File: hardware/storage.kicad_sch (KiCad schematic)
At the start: 9 parts, among them J7 Micro_SD_Card_Det1, U15 EMMC5.1_BGA153

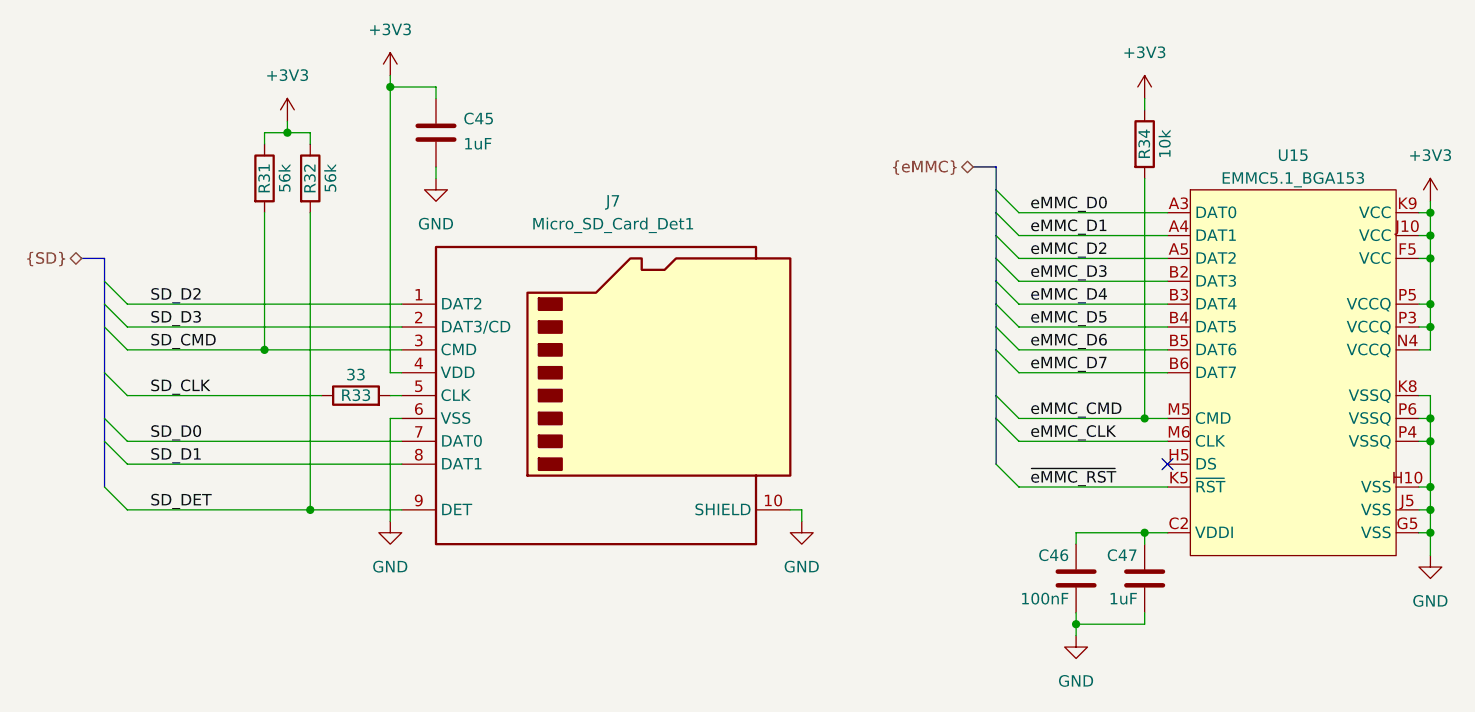
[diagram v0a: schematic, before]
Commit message: Finished DC DC converters and started decoupling the CPU
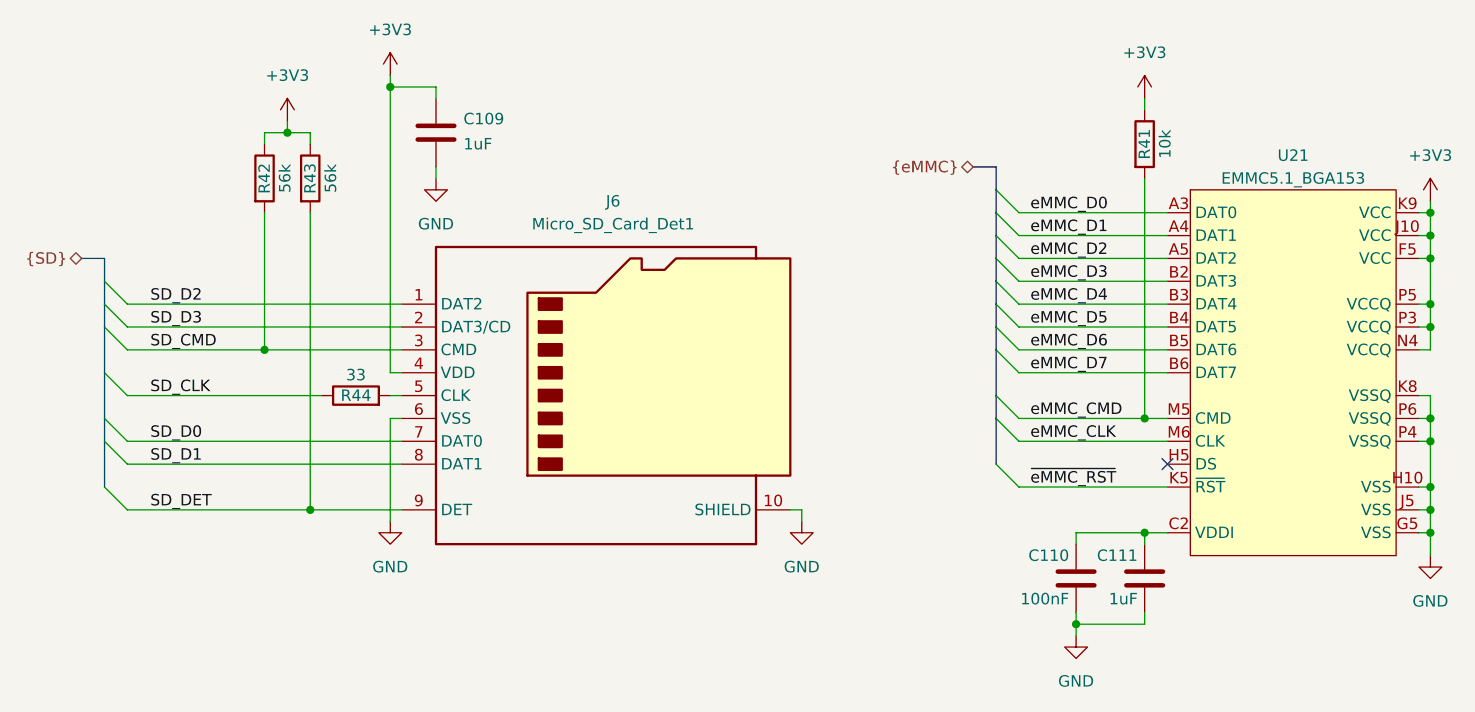
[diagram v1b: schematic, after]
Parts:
- renumbered C45 to C109, C46 to C110, C47 to C111, J7 to J6, R34 to R41, R31 to R42, R32 to R43, R33 to R44, U15 to U21
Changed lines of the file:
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@@
 		(dnp no)
 		(fields_autoplaced yes)
-		(property "Reference" "#PWR070"
+		(property "Reference" "#PWR0132"
 			(at 101.6 81.28 0)
 			(effects
@@
 			(project "cm0"
 				(path "/b53f5dbb-8078-4818-9e8f-fdf90ba6d854/bbbf0a3c-34ab-4b2d-85d9-faf7e9a88445"
-					(reference "#PWR070")
+					(reference "#PWR0132")
 					(unit 1)
 				)
@@
 		(on_board yes)
 		(dnp no)
-		(property "Reference" "C47"
+		(property "Reference" "C111"
 			(at 179.578 116.84 0)
 			(effects
@@
 			(project "cm0"
 				(path "/b53f5dbb-8078-4818-9e8f-fdf90ba6d854/bbbf0a3c-34ab-4b2d-85d9-faf7e9a88445"
-					(reference "C47")
+					(reference "C111")
 					(unit 1)
 				)
@@
 		(dnp no)
 		(fields_autoplaced yes)
-		(property "Reference" "#PWR073"
+		(property "Reference" "#PWR0130"
 			(at 180.34 69.85 0)
 			(effects
@@
 			(project ""
 				(path "/b53f5dbb-8078-4818-9e8f-fdf90ba6d854/bbbf0a3c-34ab-4b2d-85d9-faf7e9a88445"
-					(reference "#PWR073")
+					(reference "#PWR0130")
 					(unit 1)
 				)
@@
 		(on_board yes)
 		(dnp no)
-		(property "Reference" "R34"
+		(property "Reference" "R41"
 			(at 180.34 71.12 90)
 			(effects
@@
 			(project "cm0"
 				(path "/b53f5dbb-8078-4818-9e8f-fdf90ba6d854/bbbf0a3c-34ab-4b2d-85d9-faf7e9a88445"
-					(reference "R34")
+					(reference "R41")
 					(unit 1)
 				)
@@
 		(on_board yes)
 		(dnp no)
-		(property "Reference" "R31"
+		(property "Reference" "R42"
 			(at 82.55 74.93 90)
 			(effects
@@
 			(project "cm0"
 				(path "/b53f5dbb-8078-4818-9e8f-fdf90ba6d854/bbbf0a3c-34ab-4b2d-85d9-faf7e9a88445"
-					(reference "R31")
+					(reference "R42")
 					(unit 1)
 				)
@@
 		(on_board yes)
 		(dnp no)
-		(property "Reference" "C46"
+		(property "Reference" "C110"
 			(at 171.958 116.84 0)
 			(effects
@@
 			(project "cm0"
 				(path "/b53f5dbb-8078-4818-9e8f-fdf90ba6d854/bbbf0a3c-34ab-4b2d-85d9-faf7e9a88445"
-					(reference "C46")
+					(reference "C110")
 					(unit 1)
 				)
@@
 		(dnp no)
 		(fields_autoplaced yes)
-		(property "Reference" "#PWR071"
+		(property "Reference" "#PWR0135"
 			(at 142.24 119.38 0)
 			(effects
@@
 			(project ""
 				(path "/b53f5dbb-8078-4818-9e8f-fdf90ba6d854/bbbf0a3c-34ab-4b2d-85d9-faf7e9a88445"
-					(reference "#PWR071")
+					(reference "#PWR0135")
 					(unit 1)
 				)
@@
 		(dnp no)
 		(fields_autoplaced yes)
-		(property "Reference" "J7"
+		(property "Reference" "J6"
 			(at 121.285 77.47 0)
 			(effects
@@
 			(project ""
 				(path "/b53f5dbb-8078-4818-9e8f-fdf90ba6d854/bbbf0a3c-34ab-4b2d-85d9-faf7e9a88445"
-					(reference "J7")
+					(reference "J6")
 					(unit 1)
 				)
@@
 		(dnp no)
 		(fields_autoplaced yes)
-		(property "Reference" "#PWR074"
+		(property "Reference" "#PWR0133"
 			(at 212.09 81.28 0)
 			(effects
@@
 			(project "cm0"
 				(path "/b53f5dbb-8078-4818-9e8f-fdf90ba6d854/bbbf0a3c-34ab-4b2d-85d9-faf7e9a88445"
-					(reference "#PWR074")
+					(reference "#PWR0133")
 					(unit 1)
 				)
@@
 		(dnp no)
 		(fields_autoplaced yes)
-		(property "Reference" "#PWR069"
+		(property "Reference" "#PWR0134"
 			(at 96.52 119.38 0)
 			(effects
@@
 			(project ""
 				(path "/b53f5dbb-8078-4818-9e8f-fdf90ba6d854/bbbf0a3c-34ab-4b2d-85d9-faf7e9a88445"
-					(reference "#PWR069")
+					(reference "#PWR0134")
 					(unit 1)
 				)
@@
 		(dnp no)
 		(fields_autoplaced yes)
-		(property "Reference" "#PWR067"
+		(property "Reference" "#PWR0131"
 			(at 85.09 72.39 0)
 			(effects
@@
 			(project ""
 				(path "/b53f5dbb-8078-4818-9e8f-fdf90ba6d854/bbbf0a3c-34ab-4b2d-85d9-faf7e9a88445"
-					(reference "#PWR067")
+					(reference "#PWR0131")
 					(unit 1)
 				)
@@
 		(on_board yes)
 		(dnp no)
-		(property "Reference" "R33"
+		(property "Reference" "R44"
 			(at 92.71 99.06 90)
 			(effects
@@
 			(project "cm0"
 				(path "/b53f5dbb-8078-4818-9e8f-fdf90ba6d854/bbbf0a3c-34ab-4b2d-85d9-faf7e9a88445"
-					(reference "R33")
+					(reference "R44")
 					(unit 1)
 				)
@@
 		(dnp no)
 		(fields_autoplaced yes)
-		(property "Reference" "#PWR068"
+		(property "Reference" "#PWR0129"
 			(at 96.52 67.31 0)
 			(effects
@@
 			(project "cm0"
 				(path "/b53f5dbb-8078-4818-9e8f-fdf90ba6d854/bbbf0a3c-34ab-4b2d-85d9-faf7e9a88445"
-					(reference "#PWR068")
+					(reference "#PWR0129")
 					(unit 1)
 				)
@@
 		(dnp no)
 		(fields_autoplaced yes)
-		(property "Reference" "#PWR075"
+		(property "Reference" "#PWR0136"
 			(at 212.09 123.19 0)
 			(effects
@@
 			(project "cm0"
 				(path "/b53f5dbb-8078-4818-9e8f-fdf90ba6d854/bbbf0a3c-34ab-4b2d-85d9-faf7e9a88445"
-					(reference "#PWR075")
+					(reference "#PWR0136")
 					(unit 1)
 				)
@@
 		(dnp no)
 		(fields_autoplaced yes)
-		(property "Reference" "#PWR072"
+		(property "Reference" "#PWR0137"
 			(at 172.72 132.08 0)
 			(effects
@@
 			(project ""
 				(path "/b53f5dbb-8078-4818-9e8f-fdf90ba6d854/bbbf0a3c-34ab-4b2d-85d9-faf7e9a88445"
-					(reference "#PWR072")
+					(reference "#PWR0137")
 					(unit 1)
 				)
@@
 		(on_board yes)
 		(dnp no)
-		(property "Reference" "R32"
+		(property "Reference" "R43"
 			(at 87.63 74.93 90)
 			(effects
@@
 			(project "cm0"
 				(path "/b53f5dbb-8078-4818-9e8f-fdf90ba6d854/bbbf0a3c-34ab-4b2d-85d9-faf7e9a88445"
-					(reference "R32")
+					(reference "R43")
 					(unit 1)
 				)
@@
 		(dnp no)
 		(fields_autoplaced yes)
-		(property "Reference" "U15"
+		(property "Reference" "U21"
 			(at 196.85 72.39 0)
 			(effects
@@
 			(project ""
 				(path "/b53f5dbb-8078-4818-9e8f-fdf90ba6d854/bbbf0a3c-34ab-4b2d-85d9-faf7e9a88445"
-					(reference "U15")
+					(reference "U21")
 					(unit 1)
 				)
@@
 		(on_board yes)
 		(dnp no)
-		(property "Reference" "C45"
+		(property "Reference" "C109"
 			(at 104.648 68.326 0)
 			(effects
@@
 			(project "cm0"
 				(path "/b53f5dbb-8078-4818-9e8f-fdf90ba6d854/bbbf0a3c-34ab-4b2d-85d9-faf7e9a88445"
-					(reference "C45")
-					(unit 1)
-				)
+					(reference "C109")
+					(unit 1)
+				)

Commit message: Decoupling on PCB side almost done
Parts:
- J6: FT Position Offset (none) -> -1.905,0
- R44: LCSC Part # (none) -> C25105
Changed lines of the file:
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@@
+			)
+		)
+		(property "FT Position Offset" ""
+			(at 180.34 119.38 0)
+			(effects
+				(font
+					(size 1.27 1.27)
+				)
+				(hide yes)
+			)
+		)
+		(property "FT Rotation Offset" ""
+			(at 180.34 119.38 0)
+			(effects
+				(font
+					(size 1.27 1.27)
+				)
+				(hide yes)
 			)
 		)
@@
 			)
 		)
+		(property "FT Position Offset" ""
+			(at 180.34 71.12 90)
+			(effects
+				(font
+					(size 1.27 1.27)
+				)
+				(hide yes)
+			)
+		)
+		(property "FT Rotation Offset" ""
+			(at 180.34 71.12 90)
+			(effects
+				(font
+					(size 1.27 1.27)
+				)
+				(hide yes)
+			)
+		)
 		(pin "1"
 		)
@@
 		)
 		(property "LCSC Part #" "C25796"
+			(at 82.55 74.93 90)
+			(effects
+				(font
+					(size 1.27 1.27)
+				)
+				(hide yes)
+			)
+		)
+		(property "FT Position Offset" ""
+			(at 82.55 74.93 90)
+			(effects
+				(font
+					(size 1.27 1.27)
+				)
+				(hide yes)
+			)
+		)
+		(property "FT Rotation Offset" ""
 			(at 82.55 74.93 90)
 			(effects
@@
 			)
 		)
+		(property "FT Position Offset" ""
+			(at 172.72 119.38 0)
+			(effects
+				(font
+					(size 1.27 1.27)
+				)
+				(hide yes)
+			)
+		)
+		(property "FT Rotation Offset" ""
+			(at 172.72 119.38 0)
+			(effects
+				(font
+					(size 1.27 1.27)
+				)
+				(hide yes)
+			)
+		)
 		(pin "2"
 		)
@@
 			)
 		)
+		(property "FT Position Offset" "-1.905,0"
+			(at 120.65 99.06 0)
+			(effects
+				(font
+					(size 1.27 1.27)
+				)
+				(hide yes)
+			)
+		)
+		(property "FT Rotation Offset" ""
+			(at 120.65 99.06 0)
+			(effects
+				(font
+					(size 1.27 1.27)
+				)
+				(hide yes)
+			)
+		)
 		(pin "9"
 		)
@@
 			)
 		)
-		(property "LCSC Part #" ""
+		(property "LCSC Part #" "C25105"
+			(at 92.71 99.06 90)
+			(effects
+				(font
+					(size 1.27 1.27)
+				)
+				(hide yes)
+			)
+		)
+		(property "FT Position Offset" ""
+			(at 92.71 99.06 90)
+			(effects
+				(font
+					(size 1.27 1.27)
+				)
+				(hide yes)
+			)
+		)
+		(property "FT Rotation Offset" ""
 			(at 92.71 99.06 90)
 			(effects
@@
 			)
 		)
+		(property "FT Position Offset" ""
+			(at 87.63 74.93 90)
+			(effects
+				(font
+					(size 1.27 1.27)
+				)
+				(hide yes)
+			)
+		)
+		(property "FT Rotation Offset" ""
+			(at 87.63 74.93 90)
+			(effects
+				(font
+					(size 1.27 1.27)
+				)
+				(hide yes)
+			)
+		)
 		(pin "1"
 		)
@@
 			)
 		)
+		(property "FT Position Offset" ""
+			(at 196.85 96.52 0)
+			(effects
+				(font
+					(size 1.27 1.27)
+				)
+				(hide yes)
+			)
+		)
+		(property "FT Rotation Offset" ""
+			(at 196.85 96.52 0)
+			(effects
+				(font
+					(size 1.27 1.27)
+				)
+				(hide yes)
+			)
+		)
 		(pin "B6"
 		)
@@
 			(at 101.6 69.85 0)
 			(effects
+				(font
+					(size 1.27 1.27)
+				)
+				(hide yes)
+			)
+		)
+		(property "FT Position Offset" ""
+			(at 101.6 69.85 0)
+			(effects
+				(font
+					(size 1.27 1.27)
+				)
+				(hide yes)
+			)
+		)
+		(property "FT Rotation Offset" ""
+			(at 101.6 69.85 0)
+			(effects

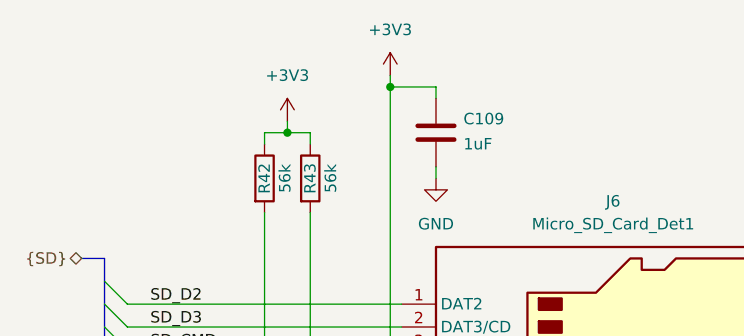
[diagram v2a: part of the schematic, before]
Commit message: Routed DCDC, EPHY and SD
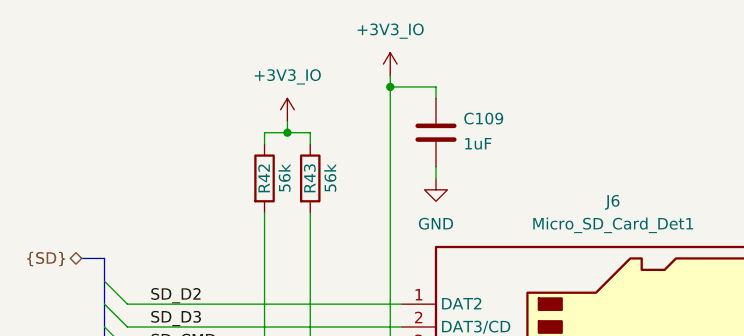
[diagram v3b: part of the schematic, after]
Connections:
- net +3V3: no longer C109.2, J6.4 (VDD), R42.1, R43.1
- new net +3V3_IO: C109.2, J6.4 (VDD), R42.1, R43.1
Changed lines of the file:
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@@
+	)
+	(symbol
+		(lib_id "cm0:+3V3_IO")
+		(at 85.09 68.58 0)
+		(unit 1)
+		(exclude_from_sim no)
+		(in_bom yes)
+		(on_board yes)
+		(dnp no)
+		(fields_autoplaced yes)
+		(property "Reference" "#PWR0131"
+			(at 85.09 72.39 0)
+			(effects
+				(font
+					(size 1.27 1.27)
+				)
+				(hide yes)
+			)
+		)
+		(property "Value" "+3V3_IO"
+			(at 85.09 63.5 0)
+			(effects
+				(font
+					(size 1.27 1.27)
+				)
+			)
+		)
+		(property "Footprint" ""
+			(at 85.09 68.58 0)
+			(effects
+				(font
+					(size 1.27 1.27)
+				)
+				(hide yes)
+			)
+		)
+		(property "Datasheet" ""
+			(at 85.09 68.58 0)
+			(effects
+				(font
+					(size 1.27 1.27)
+				)
+				(hide yes)
+			)
+		)
+		(property "Description" "Power symbol creates a global label with name \"+3V3_IO\""
+			(at 85.09 68.58 0)
+			(effects
+				(font
+					(size 1.27 1.27)
+				)
+				(hide yes)
+			)
+		)
+		(pin "1"
+		)
+		(instances
+			(project "cm0"
+				(path "/b53f5dbb-8078-4818-9e8f-fdf90ba6d854/bbbf0a3c-34ab-4b2d-85d9-faf7e9a88445"
+					(reference "#PWR0131")
+					(unit 1)
+				)
+			)
+		)
 	)
 	(symbol
@@
 	)
 	(symbol
-		(lib_id "power:+3V3")
-		(at 85.09 68.58 0)
-		(unit 1)
-		(exclude_from_sim no)
-		(in_bom yes)
-		(on_board yes)
-		(dnp no)
-		(fields_autoplaced yes)
-		(property "Reference" "#PWR0131"
-			(at 85.09 72.39 0)
-			(effects
-				(font
-					(size 1.27 1.27)
-				)
-				(hide yes)
-			)
-		)
-		(property "Value" "+3V3"
-			(at 85.09 63.5 0)
-			(effects
-				(font
-					(size 1.27 1.27)
-				)
-			)
-		)
-		(property "Footprint" ""
-			(at 85.09 68.58 0)
-			(effects
-				(font
-					(size 1.27 1.27)
-				)
-				(hide yes)
-			)
-		)
-		(property "Datasheet" ""
-			(at 85.09 68.58 0)
-			(effects
-				(font
-					(size 1.27 1.27)
-				)
-				(hide yes)
-			)
-		)
-		(property "Description" "Power symbol creates a global label with name \"+3V3\""
-			(at 85.09 68.58 0)
-			(effects
-				(font
-					(size 1.27 1.27)
-				)
-				(hide yes)
-			)
-		)
-		(pin "1"
-		)
-		(instances
-			(project ""
-				(path "/b53f5dbb-8078-4818-9e8f-fdf90ba6d854/bbbf0a3c-34ab-4b2d-85d9-faf7e9a88445"
-					(reference "#PWR0131")
-					(unit 1)
-				)
-			)
-		)
-	)
-	(symbol
-		(lib_id "Device:R")
-		(at 92.71 99.06 90)
-		(unit 1)
-		(exclude_from_sim no)
-		(in_bom yes)
-		(on_board yes)
-		(dnp no)
-		(property "Reference" "R44"
-			(at 92.71 99.06 90)
-			(effects
-				(font
-					(size 1.27 1.27)
-				)
-			)
-		)
-		(property "Value" "33"
-			(at 92.71 96.774 90)
-			(effects
-				(font
-					(size 1.27 1.27)
-				)
-			)
-		)
-		(property "Footprint" "Resistor_SMD:R_0402_1005Metric"
-			(at 92.71 100.838 90)
-			(effects
-				(font
-					(size 1.27 1.27)
-				)
-				(hide yes)
-			)
-		)
-		(property "Datasheet" "~"
-			(at 92.71 99.06 0)
-			(effects
-				(font
-					(size 1.27 1.27)
-				)
-				(hide yes)
-			)
-		)
-		(property "Description" "Resistor"
-			(at 92.71 99.06 0)
-			(effects
-				(font
-					(size 1.27 1.27)
-				)
-				(hide yes)
-			)
-		)
-		(property "LCSC Part #" "C25105"
-			(at 92.71 99.06 90)
-			(effects
-				(font
-					(size 1.27 1.27)
-				)
-				(hide yes)
-			)
-		)
-		(property "FT Position Offset" ""
-			(at 92.71 99.06 90)
-			(effects
-				(font
-					(size 1.27 1.27)
-				)
-				(hide yes)
-			)
-		)
-		(property "FT Rotation Offset" ""
-			(at 92.71 99.06 90)
-			(effects
-				(font
-					(size 1.27 1.27)
-				)
-				(hide yes)
-			)
-		)
-		(pin "1"
-		)
-		(pin "2"
-		)
-		(instances
-			(project "cm0"
-				(path "/b53f5dbb-8078-4818-9e8f-fdf90ba6d854/bbbf0a3c-34ab-4b2d-85d9-faf7e9a88445"
-					(reference "R44")
-					(unit 1)
-				)
-			)
-		)
-	)
-	(symbol
-		(lib_id "power:+3V3")
+		(lib_id "cm0:+3V3_IO")
 		(at 96.52 63.5 0)
 		(unit 1)
@@
 			)
 		)
-		(property "Value" "+3V3"
+		(property "Value" "+3V3_IO"
 			(at 96.52 58.42 0)
 			(effects
@@
 			)
 		)
-		(property "Description" "Power symbol creates a global label with name \"+3V3\""
+		(property "Description" "Power symbol creates a global label with name \"+3V3_IO\""
 			(at 96.52 63.5 0)
 			(effects
@@
 		)
 		(instances
+			(project ""
+				(path "/b53f5dbb-8078-4818-9e8f-fdf90ba6d854/bbbf0a3c-34ab-4b2d-85d9-faf7e9a88445"
+					(reference "#PWR0129")
+					(unit 1)
+				)
+			)
+		)
+	)
+	(symbol
+		(lib_id "Device:R")
+		(at 92.71 99.06 90)
+		(unit 1)
+		(exclude_from_sim no)
+		(in_bom yes)
+		(on_board yes)
+		(dnp no)
+		(property "Reference" "R44"
+			(at 92.71 99.06 90)
+			(effects
+				(font
+					(size 1.27 1.27)
+				)
+			)
+		)
+		(property "Value" "33"
+			(at 92.71 96.774 90)
+			(effects
+				(font
+					(size 1.27 1.27)
+				)
+			)
+		)
+		(property "Footprint" "Resistor_SMD:R_0402_1005Metric"
+			(at 92.71 100.838 90)
+			(effects
+				(font
+					(size 1.27 1.27)
+				)
+				(hide yes)
+			)
+		)
+		(property "Datasheet" "~"
+			(at 92.71 99.06 0)
+			(effects
+				(font
+					(size 1.27 1.27)
+				)
+				(hide yes)
+			)
+		)
+		(property "Description" "Resistor"
+			(at 92.71 99.06 0)
+			(effects
+				(font
+					(size 1.27 1.27)
+				)
+				(hide yes)
+			)
+		)
+		(property "LCSC Part #" "C25105"
+			(at 92.71 99.06 90)
+			(effects
+				(font
+					(size 1.27 1.27)
+				)
+				(hide yes)
+			)
+		)
+		(property "FT Position Offset" ""
+			(at 92.71 99.06 90)
+			(effects
+				(font
+					(size 1.27 1.27)
+				)
+				(hide yes)
+			)
+		)
+		(property "FT Rotation Offset" ""
+			(at 92.71 99.06 90)
+			(effects
+				(font
+					(size 1.27 1.27)
+				)
+				(hide yes)
+			)
+		)
+		(pin "1"
+		)
+		(pin "2"
+		)
+		(instances
 			(project "cm0"
 				(path "/b53f5dbb-8078-4818-9e8f-fdf90ba6d854/bbbf0a3c-34ab-4b2d-85d9-faf7e9a88445"
-					(reference "#PWR0129")
-					(unit 1)
-				)
+					(reference "R44")
+					(unit 1)
+				)
